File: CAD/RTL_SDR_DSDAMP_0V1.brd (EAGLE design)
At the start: 33.7 x 22 mm, 45 parts, among them U1 THS4521ID, U2 TPS73601DBVR, U3 BGA416, LNA

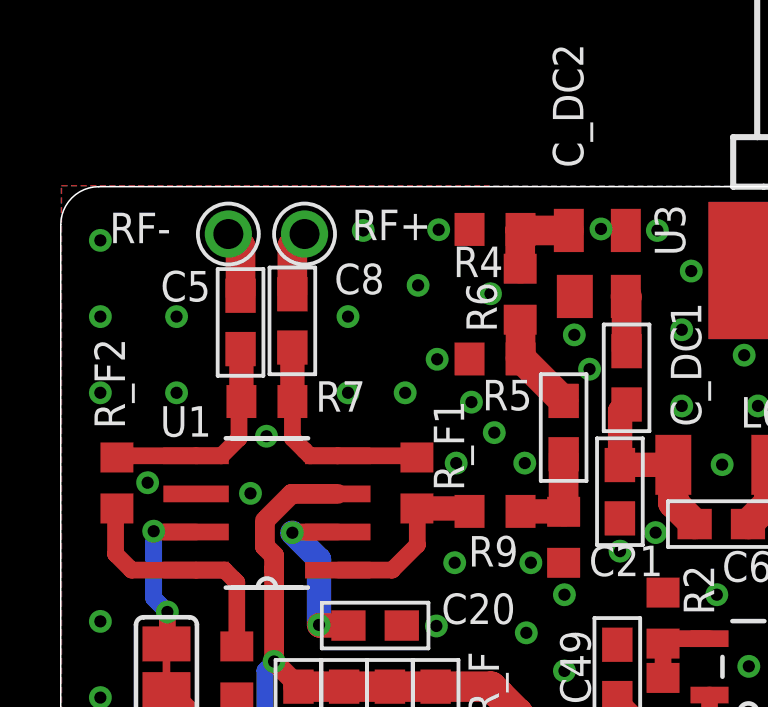
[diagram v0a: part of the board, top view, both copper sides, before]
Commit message: Adding the missing LNA VDD bias network, updating CAD / CAM / PDF files
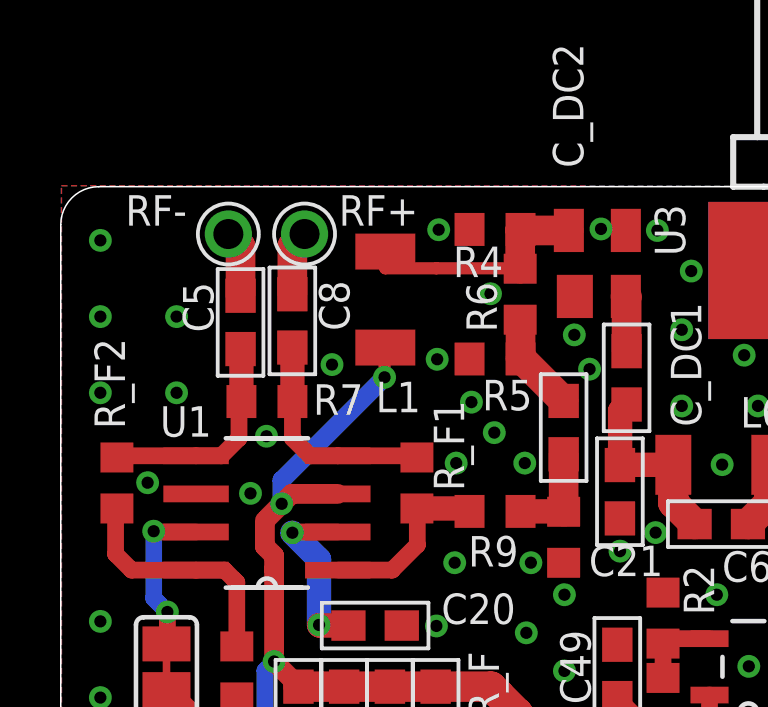
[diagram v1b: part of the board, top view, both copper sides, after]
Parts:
- added L1: 47uH, dzo:L1210
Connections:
- net N$2: now also L1.2
- net VDD_3V3: now also L1.1
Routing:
- net VDD_3V3: track 32.0 -> 38.7 mm, vias 2 -> 4
- net N$2: track 2.94 -> 8.01 mm
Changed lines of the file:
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@@
 <setting verticaltext="up"/>
 </settings>
-<grid distance="25" unitdist="mil" unit="mil" style="dots" multiple="1" display="yes" altdistance="1" altunitdist="mil" altunit="mil"/>
+<grid distance="5" unitdist="mil" unit="mil" style="dots" multiple="1" display="yes" altdistance="1" altunitdist="mil" altunit="mil"/>
 <layers>
 <layer number="1" name="Top" color="4" fill="1" visible="yes" active="yes"/>
@@
 </element>
 <element name="R7" library="resistor" package="R0603" value="500" x="6.874" y="14.838" smashed="yes" rot="R180">
-<attribute name="NAME" x="8.493" y="14.499" size="1.016" layer="25" font="vector" ratio="15"/>
+<attribute name="NAME" x="8.4168" y="14.3974" size="1.016" layer="25" font="vector" ratio="15"/>
 <attribute name="VALUE" x="7.763" y="16.87" size="1.27" layer="27" rot="R180"/>
 </element>
 <element name="C5" library="dzo" package="0603" value="220nF" x="5.9944" y="17.4752" smashed="yes" rot="R270">
-<attribute name="NAME" x="3.3274" y="18.1742" size="1.016" layer="25" font="vector" ratio="15"/>
+<attribute name="NAME" x="5.0922" y="17.145" size="1.016" layer="25" font="vector" ratio="15" rot="R90"/>
 <attribute name="VALUE" x="5.4864" y="18.9992" size="1.016" layer="27" rot="R270"/>
 </element>
 <element name="C8" library="dzo" package="0603" value="220nF" x="7.7216" y="17.526" smashed="yes" rot="R270">
-<attribute name="NAME" x="9.1186" y="18.415" size="1.016" layer="25" font="vector" ratio="15"/>
+<attribute name="NAME" x="9.6266" y="17.1958" size="1.016" layer="25" font="vector" ratio="15" rot="R90"/>
 <attribute name="VALUE" x="7.2136" y="19.05" size="1.016" layer="27" rot="R270"/>
 </element>
@@
 </element>
 <element name="RF+" library="dzo" package="TESTPOINT1,0" value="TESTPOINT39MIL" x="8.128" y="20.4216" smashed="yes" rot="R270">
-<attribute name="NAME" x="9.7028" y="20.2184" size="1.016" layer="25" font="vector" ratio="15"/>
+<attribute name="NAME" x="9.271" y="20.701" size="1.016" layer="25" font="vector" ratio="15"/>
 </element>
 <element name="RF-" library="dzo" package="TESTPOINT1,0" value="TESTPOINT39MIL" x="5.588" y="20.4216" smashed="yes">
-<attribute name="NAME" x="1.6256" y="20.1168" size="1.016" layer="25" font="vector" ratio="15"/>
+<attribute name="NAME" x="2.159" y="20.701" size="1.016" layer="25" font="vector" ratio="15"/>
 </element>
 <element name="B+" library="dzo" package="TESTPOINT1,0" value="TESTPOINT39MIL" x="32.1564" y="4.572" smashed="yes">
@@
 <element name="B-" library="dzo" package="TESTPOINT1,0" value="TESTPOINT39MIL" x="32.1564" y="7.112" smashed="yes" rot="R90">
 <attribute name="NAME" x="31.7246" y="8.2296" size="1.016" layer="25" font="vector" ratio="15"/>
+</element>
+<element name="L1" library="dzo" package="L1210" value="47uH" x="10.8204" y="18.2372" smashed="yes" rot="R90">
+<attribute name="MANUF" value="TDK" x="10.8204" y="18.2372" size="1.778" layer="27" rot="R90" display="off"/>
+<attribute name="MANUFNR" value="NLCV32 series" x="10.8204" y="18.2372" size="1.778" layer="27" rot="R90" display="off"/>
+<attribute name="DESCR" value="Inductor, wirewound" x="10.8204" y="18.2372" size="1.778" layer="27" rot="R90" display="off"/>
+<attribute name="NAME" x="10.503" y="14.4812" size="1.016" layer="25" font="vector" ratio="20"/>
+<attribute name="VALUE" x="13.6954" y="15.2322" size="1.27" layer="27" rot="R90"/>
 </element>
 </elements>
@@
 <via x="10.990678125" y="2.366975" extent="1-16" drill="0.4064"/>
 <via x="12.514678125" y="2.366975" extent="1-16" drill="0.4064"/>
-<via x="11.913459375" y="18.710978125" extent="1-16" drill="0.4064"/>
 <via x="16.790259375" y="8.398578125" extent="1-16" drill="0.4064"/>
 <via x="15.672659375" y="9.465378125" extent="1-16" drill="0.4064"/>
@@
 <via x="25.137778125" y="3.2893" extent="1-16" drill="0.4064"/>
 <via x="28.744578125" y="3.2893" extent="1-16" drill="0.4064"/>
-<via x="10.084659375" y="20.539778125" extent="1-16" drill="0.4064"/>
 <via x="2.464659375" y="2.759778125" extent="1-16" drill="0.4064"/>
 <via x="4.572859375" y="1.515178125" extent="1-16" drill="0.4064"/>
@@
 <via x="6.477859375" y="1.515178125" extent="1-16" drill="0.4064"/>
 <via x="15.520259375" y="7.128578125" extent="1-16" drill="0.4064"/>
-<via x="9.576659375" y="17.669578125" extent="1-16" drill="0.4064"/>
-<via x="9.576659375" y="15.129578125" extent="1-16" drill="0.4064"/>
-<via x="11.481659375" y="15.129578125" extent="1-16" drill="0.4064"/>
+<via x="9.043259375" y="16.069378125" extent="1-16" drill="0.4064"/>
 </signal>
 <signal name="N$15">
@@
 <wire x1="7.112" y1="9.7028" x2="6.8072" y2="10.0076" width="0.6604" layer="1"/>
 <wire x1="9.2362" y1="11.759" x2="7.695" y2="11.759" width="0.6604" layer="1"/>
-<wire x1="7.695" y1="11.759" x2="6.9088" y2="10.9728" width="0.6604" layer="1"/>
+<wire x1="7.695" y1="11.759" x2="7.366" y2="11.43" width="0.6604" layer="1"/>
+<wire x1="7.366" y1="11.43" x2="6.9088" y2="10.9728" width="0.6604" layer="1"/>
 <wire x1="6.9088" y1="10.9728" x2="6.8072" y2="10.8712" width="0.5588" layer="1"/>
 <wire x1="6.8072" y1="10.8712" x2="6.8072" y2="10.0076" width="0.6604" layer="1"/>
+<contactref element="L1" pad="1"/>
+<wire x1="10.8204" y1="16.6372" x2="10.795" y2="16.6118" width="0.4064" layer="1"/>
+<wire x1="10.795" y1="16.6118" x2="10.795" y2="15.6464" width="0.4064" layer="1"/>
+<via x="10.795" y="15.6464" extent="1-16" drill="0.4064"/>
+<wire x1="10.795" y1="15.6464" x2="7.366" y2="12.2174" width="0.6096" layer="16"/>
+<wire x1="7.366" y1="12.2174" x2="7.366" y2="11.43" width="0.6096" layer="16"/>
+<via x="7.366" y="11.43" extent="1-16" drill="0.4064"/>
 </signal>
 <signal name="N$1">
@@
 <wire x1="15.328" y1="20.574" x2="15.3162" y2="20.5622" width="0.9906" layer="1"/>
 <wire x1="15.3162" y1="20.5622" x2="15.3162" y2="19.265" width="0.9906" layer="1"/>
+<contactref element="L1" pad="2"/>
+<wire x1="10.8204" y1="19.8372" x2="10.8204" y2="19.2786" width="0.4064" layer="1"/>
+<wire x1="10.8204" y1="19.2786" x2="12.5222" y2="19.2786" width="0.4064" layer="1"/>
+<wire x1="12.5222" y1="19.2786" x2="15.3162" y2="19.2786" width="0.4064" layer="1"/>
+<wire x1="15.3162" y1="19.2786" x2="15.3162" y2="19.265" width="0.4064" layer="1"/>
 </signal>
 <signal name="N$4">
